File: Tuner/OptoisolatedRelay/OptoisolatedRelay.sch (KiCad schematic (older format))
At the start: 94 parts, among them J1 Conn_02x05_Odd_Even, J10 Conn_01x02, J11 Conn_01x02, J12 Conn_01x01, J13 Conn_01x01, J14 Conn_01x02, J15 Conn_01x02, J16 Conn_01x02, J17 Conn_01x02, J18 Conn_01x02, J19 Conn_01x02, J2 Conn_01x02, J20 Conn_01x02, J21 Conn_01x02, J22 Conn_01x02, J3 Conn_01x01, J4 Conn_01x01, J5 Conn_01x02, J6 Conn_01x02, J7 Conn_01x02, J8 Conn_01x02, J9 Conn_01x02, U1 MCP23017, U10 PC817, U11 PC817, U12 PC817, U13 PC817, U14 PC817, U15 PC817, U16 PC817, U17 PC817, U18 PC817, U19 PC817, U2 ULN2803A, U3 ULN2803A, U4 PC817, U5 PC817, U6 PC817, U7 PC817, U8 PC817, U9 PC817

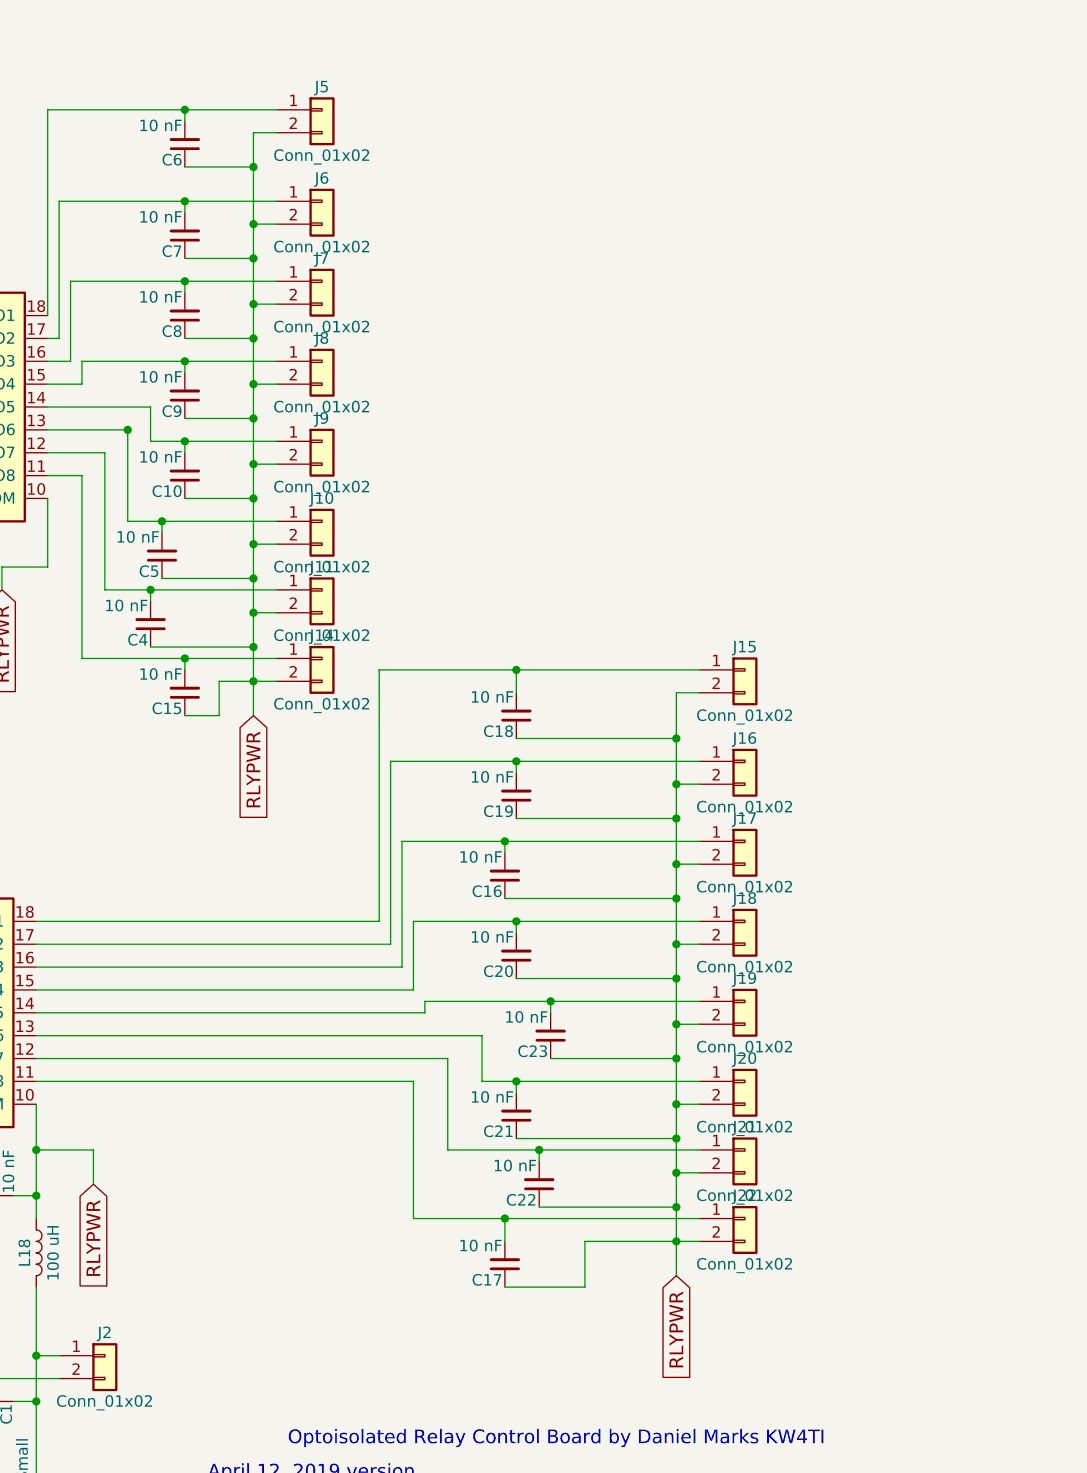
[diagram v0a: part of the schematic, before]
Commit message: Added LEDs to OptoisolatedRelay
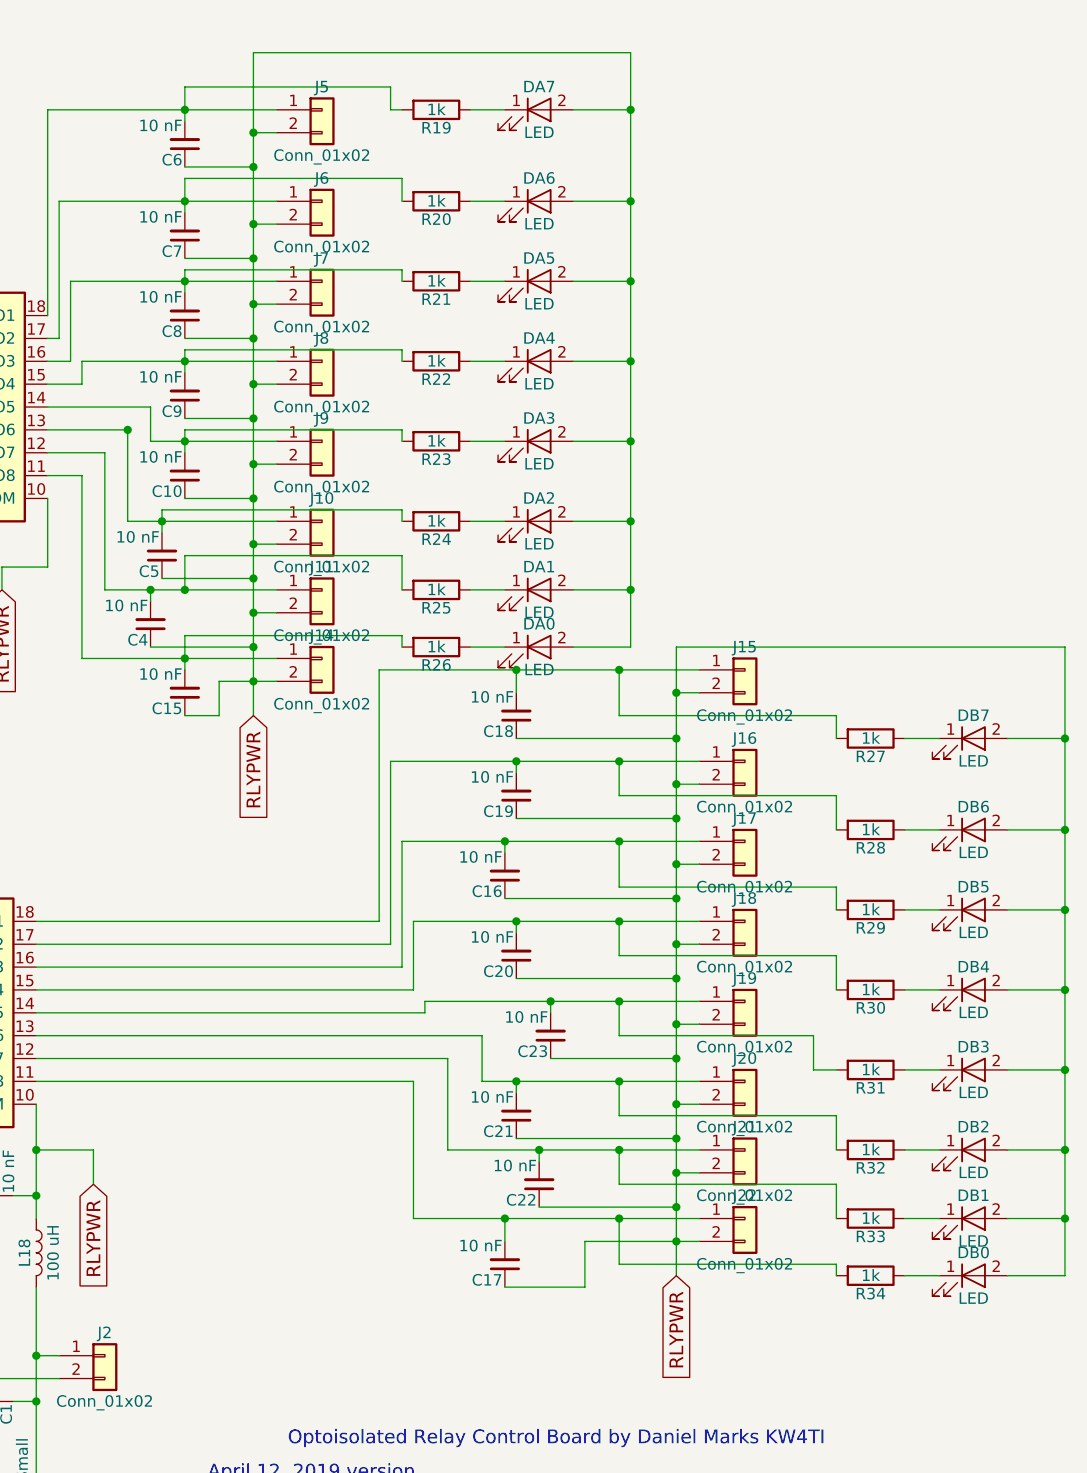
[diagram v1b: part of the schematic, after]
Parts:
- added DA0, DA1, DA2, DA3, DA4, DA5, DA6, DA7, DB0, DB1, DB2, DB3, DB4, DB5, DB6, DB7: LED, LEDs:LED_D3.0mm, symbol LED
- added R19, R20, R21, R22, R23, R24, R25, R26, R27, R28, R29, R30, R31, R32, R33, R34: 1k, Resistors_THT:R_Axial_DIN0207_L6.3mm_D2.5mm_P7.62mm_Horizontal, symbol R
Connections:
- net RLYPWR: now also DA0.2 (A), DA1.2 (A), DA2.2 (A), DA3.2 (A), DA4.2 (A), DA5.2 (A), DA6.2 (A), DA7.2 (A), DB0.2 (A), DB1.2 (A), DB2.2 (A), DB3.2 (A), DB4.2 (A), DB5.2 (A), DB6.2 (A), DB7.2 (A)
- net at C15.2, J14.1 (Pin_1), U2.11 (O8): now also R26.2
- net at C4.2, J11.1 (Pin_1), U2.12 (O7): now also R25.2
- net at C5.2, J10.1 (Pin_1), U2.13 (O6): now also R24.2
- net at C10.2, J9.1 (Pin_1), U2.14 (O5): now also R23.2
- net at C9.2, J8.1 (Pin_1), U2.15 (O4): now also R22.2
- net at C8.2, J7.1 (Pin_1), U2.16 (O3): now also R21.2
- net at C7.2, J6.1 (Pin_1), U2.17 (O2): now also R20.2
- net at C6.2, J5.1 (Pin_1), U2.18 (O1): now also R19.2
- net at C17.2, J22.1 (Pin_1), U3.11 (O8): now also R34.2
- net at C22.2, J21.1 (Pin_1), U3.12 (O7): now also R33.2
- net at C21.2, J20.1 (Pin_1), U3.13 (O6): now also R32.2
- net at C23.2, J19.1 (Pin_1), U3.14 (O5): now also R31.2
- net at C20.2, J18.1 (Pin_1), U3.15 (O4): now also R30.2
- net at C16.2, J17.1 (Pin_1), U3.16 (O3): now also R29.2
- net at C19.2, J16.1 (Pin_1), U3.17 (O2): now also R28.2
- net at C18.2, J15.1 (Pin_1), U3.18 (O1): now also R27.2
- new net: DA7.1 (K), R19.1
- new net: DA6.1 (K), R20.1
- new net: DA5.1 (K), R21.1
- new net: DA4.1 (K), R22.1
- new net: DA3.1 (K), R23.1
- new net: DA2.1 (K), R24.1
- new net: DA1.1 (K), R25.1
- new net: DA0.1 (K), R26.1
- new net: DB7.1 (K), R27.1
- new net: DB6.1 (K), R28.1
- new net: DB5.1 (K), R29.1
- new net: DB4.1 (K), R30.1
- new net: DB3.1 (K), R31.1
- new net: DB2.1 (K), R32.1
- new net: DB1.1 (K), R33.1
- new net: DB0.1 (K), R34.1
